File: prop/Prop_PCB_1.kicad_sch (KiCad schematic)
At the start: 13 parts

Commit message: finalize3pcb schematic
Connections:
- net SV1 is gone; now on net Sol1Lead1: J?.1
- net SV2 is gone; now on net Sol2Lead1: J?.3
- net Sol1Lead2: now also J?.2
- net Sol2Lead2: now also J?.4
- no-connect marks 39 -> 43
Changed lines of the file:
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@@
   (no_connect (at 54.61 40.64))
   (no_connect (at 54.61 43.18))
+  (no_connect (at 54.61 55.88))
+  (no_connect (at 54.61 58.42))
+  (no_connect (at 54.61 60.96))
+  (no_connect (at 54.61 66.04))
   (no_connect (at 82.55 58.42))
   (no_connect (at 54.61 83.82))
@@
   (no_connect (at 83.82 172.72))
   (no_connect (at 262.89 63.5))
-  (polyline (pts (xy 271.78 99.06) (xy 271.78 130.81))
+  (polyline (pts (xy 273.05 99.06) (xy 273.05 130.81))
     (stroke (width 0) (type default) (color 0 0 0 0))
   )
@@
     (stroke (width 0) (type default) (color 0 0 0 0))
   )
-  (wire (pts (xy 52.705 55.88) (xy 54.61 55.88))
-    (stroke (width 0) (type default) (color 0 0 0 0))
-  )
   (wire (pts (xy 262.89 53.34) (xy 264.795 53.34))
     (stroke (width 0) (type default) (color 0 0 0 0))
@@
     (stroke (width 0) (type default) (color 0 0 0 0))
   )
-  (polyline (pts (xy 43.18 100.33) (xy 111.76 100.33))
+  (polyline (pts (xy 39.37 100.33) (xy 111.76 100.33))
     (stroke (width 0) (type default) (color 0 0 0 0))
   )
@@
     (stroke (width 0) (type default) (color 0 0 0 0))
   )
-  (polyline (pts (xy 215.9 99.06) (xy 271.78 99.06))
-    (stroke (width 0) (type default) (color 0 0 0 0))
-  )
-  (wire (pts (xy 52.705 60.96) (xy 54.61 60.96))
+  (polyline (pts (xy 215.9 99.06) (xy 273.05 99.06))
     (stroke (width 0) (type default) (color 0 0 0 0))
   )
@@
     (stroke (width 0) (type default) (color 0 0 0 0))
   )
-  (polyline (pts (xy 215.9 83.82) (xy 271.78 83.82))
+  (polyline (pts (xy 212.09 83.82) (xy 274.32 83.82))
     (stroke (width 0) (type default) (color 0 0 0 0))
   )
@@
     (stroke (width 0) (type default) (color 0 0 0 0))
   )
+  (wire (pts (xy 232.41 148.59) (xy 236.22 148.59))
+    (stroke (width 0) (type default) (color 0 0 0 0))
+  )
   (wire (pts (xy 165.1 115.57) (xy 165.1 113.03))
     (stroke (width 0) (type default) (color 0 0 0 0))
@@
     (stroke (width 0) (type default) (color 0 0 0 0))
   )
-  (polyline (pts (xy 215.9 29.21) (xy 215.9 83.82))
-    (stroke (width 0) (type default) (color 0 0 0 0))
-  )
-  (polyline (pts (xy 43.18 26.67) (xy 43.18 100.33))
-    (stroke (width 0) (type default) (color 0 0 0 0))
-  )
-  (polyline (pts (xy 271.78 29.21) (xy 215.9 29.21))
+  (polyline (pts (xy 212.09 29.21) (xy 212.09 83.82))
+    (stroke (width 0) (type default) (color 0 0 0 0))
+  )
+  (polyline (pts (xy 39.37 26.67) (xy 39.37 100.33))
+    (stroke (width 0) (type default) (color 0 0 0 0))
+  )
+  (polyline (pts (xy 274.32 29.21) (xy 212.09 29.21))
     (stroke (width 0) (type default) (color 0 0 0 0))
   )
@@
     (stroke (width 0) (type default) (color 0 0 0 0))
   )
-  (wire (pts (xy 52.705 58.42) (xy 54.61 58.42))
-    (stroke (width 0) (type default) (color 0 0 0 0))
-  )
   (wire (pts (xy 95.25 68.58) (xy 82.55 68.58))
     (stroke (width 0) (type default) (color 0 0 0 0))
@@
     (stroke (width 0) (type default) (color 0 0 0 0))
   )
-  (polyline (pts (xy 271.78 83.82) (xy 271.78 29.21))
+  (polyline (pts (xy 274.32 83.82) (xy 274.32 29.21))
     (stroke (width 0) (type default) (color 0 0 0 0))
   )
@@
     (stroke (width 0) (type default) (color 0 0 0 0))
   )
-  (wire (pts (xy 52.705 66.04) (xy 54.61 66.04))
-    (stroke (width 0) (type default) (color 0 0 0 0))
-  )
   (wire (pts (xy 172.72 73.66) (xy 172.72 77.47))
     (stroke (width 0) (type default) (color 0 0 0 0))
@@
     (stroke (width 0) (type default) (color 0 0 0 0))
   )
-  (polyline (pts (xy 271.78 130.81) (xy 215.9 130.81))
+  (polyline (pts (xy 273.05 130.81) (xy 215.9 130.81))
     (stroke (width 0) (type default) (color 0 0 0 0))
   )
@@
     (stroke (width 0) (type default) (color 0 0 0 0))
   )
-  (polyline (pts (xy 111.76 26.67) (xy 43.18 26.67))
+  (polyline (pts (xy 111.76 26.67) (xy 39.37 26.67))
     (stroke (width 0) (type default) (color 0 0 0 0))
   )
@@
     (stroke (width 0) (type default) (color 0 0 0 0))
   )
+  (wire (pts (xy 232.41 153.67) (xy 236.22 153.67))
+    (stroke (width 0) (type default) (color 0 0 0 0))
+  )
   (wire (pts (xy 74.93 127) (xy 80.01 127))
     (stroke (width 0) (type default) (color 0 0 0 0))
@@
     )
   )
-  (global_label "SV1" (shape input) (at 236.22 146.05 0) (fields_autoplaced)
-    (effects (font (size 1.27 1.27)) (justify left))
-    (property "Intersheet References" "${INTERSHEET_REFS}" (id 0) (at 242.1407 145.9706 0)
-      (effects (font (size 1.27 1.27)) (justify left) hide)
-    )
-  )
-  (global_label "SV2" (shape input) (at 236.22 151.13 0) (fields_autoplaced)
-    (effects (font (size 1.27 1.27)) (justify left))
-    (property "Intersheet References" "${INTERSHEET_REFS}" (id 0) (at 242.1407 151.0506 0)
+  (global_label "Sol1Lead1" (shape input) (at 236.22 146.05 0) (fields_autoplaced)
+    (effects (font (size 1.27 1.27)) (justify left))
+    (property "Intersheet References" "${INTERSHEET_REFS}" (id 0) (at 248.4907 145.9706 0)
+      (effects (font (size 1.27 1.27)) (justify left) hide)
+    )
+  )
+  (global_label "Sol2Lead1" (shape input) (at 236.22 151.13 0) (fields_autoplaced)
+    (effects (font (size 1.27 1.27)) (justify left))
+    (property "Intersheet References" "${INTERSHEET_REFS}" (id 0) (at 248.4907 151.0506 0)
       (effects (font (size 1.27 1.27)) (justify left) hide)
     )
@@
     )
   )
-  (global_label "CS5" (shape input) (at 52.705 66.04 180) (fields_autoplaced)
-    (effects (font (size 1.27 1.27)) (justify right))
-    (property "Intersheet References" "${INTERSHEET_REFS}" (id 0) (at 46.6029 65.9606 0)
-      (effects (font (size 1.27 1.27)) (justify right) hide)
-    )
-  )
-  (global_label "CS3" (shape input) (at 52.705 60.96 180) (fields_autoplaced)
-    (effects (font (size 1.27 1.27)) (justify right))
-    (property "Intersheet References" "${INTERSHEET_REFS}" (id 0) (at 46.6029 60.8806 0)
-      (effects (font (size 1.27 1.27)) (justify right) hide)
-    )
-  )
   (global_label "Sol1" (shape input) (at 225.425 113.03 180) (fields_autoplaced)
     (effects (font (size 1.27 1.27)) (justify right))
@@
     )
   )
-  (global_label "CS2" (shape input) (at 52.705 58.42 180) (fields_autoplaced)
-    (effects (font (size 1.27 1.27)) (justify right))
-    (property "Intersheet References" "${INTERSHEET_REFS}" (id 0) (at 46.6029 58.3406 0)
-      (effects (font (size 1.27 1.27)) (justify right) hide)
-    )
-  )
   (global_label "Sol1_33" (shape input) (at 225.425 48.26 180) (fields_autoplaced)
     (effects (font (size 1.27 1.27)) (justify right))
@@
     )
   )
-  (global_label "CS1" (shape input) (at 52.705 55.88 180) (fields_autoplaced)
-    (effects (font (size 1.27 1.27)) (justify right))
-    (property "Intersheet References" "${INTERSHEET_REFS}" (id 0) (at 46.6029 55.8006 0)
-      (effects (font (size 1.27 1.27)) (justify right) hide)
-    )
-  )
   (global_label "PWM3_33" (shape input) (at 225.425 58.42 180) (fields_autoplaced)
     (effects (font (size 1.27 1.27)) (justify right))
@@
     )
   )
+  (global_label "Sol2Lead2" (shape input) (at 236.22 153.67 0) (fields_autoplaced)
+    (effects (font (size 1.27 1.27)) (justify left))
+    (property "Intersheet References" "${INTERSHEET_REFS}" (id 0) (at 248.4907 153.5906 0)
+      (effects (font (size 1.27 1.27)) (justify left) hide)
+    )
+  )
   (global_label "SPI0_SCK" (shape input) (at 52.705 53.34 180) (fields_autoplaced)
     (effects (font (size 1.27 1.27)) (justify right))
@@
       (effects (font (size 1.27 1.27)) (justify left) hide)
     )
+  )
+  (global_label "Sol1Lead2" (shape input) (at 236.22 148.59 0) (fields_autoplaced)
+    (effects (font (size 1.27 1.27)) (justify left))
+    (property "Intersheet References" "${INTERSHEET_REFS}" (id 0) (at 248.4907 148.5106 0)
+      (effects (font (size 1.27 1.27)) (justify left) hide)
+    )

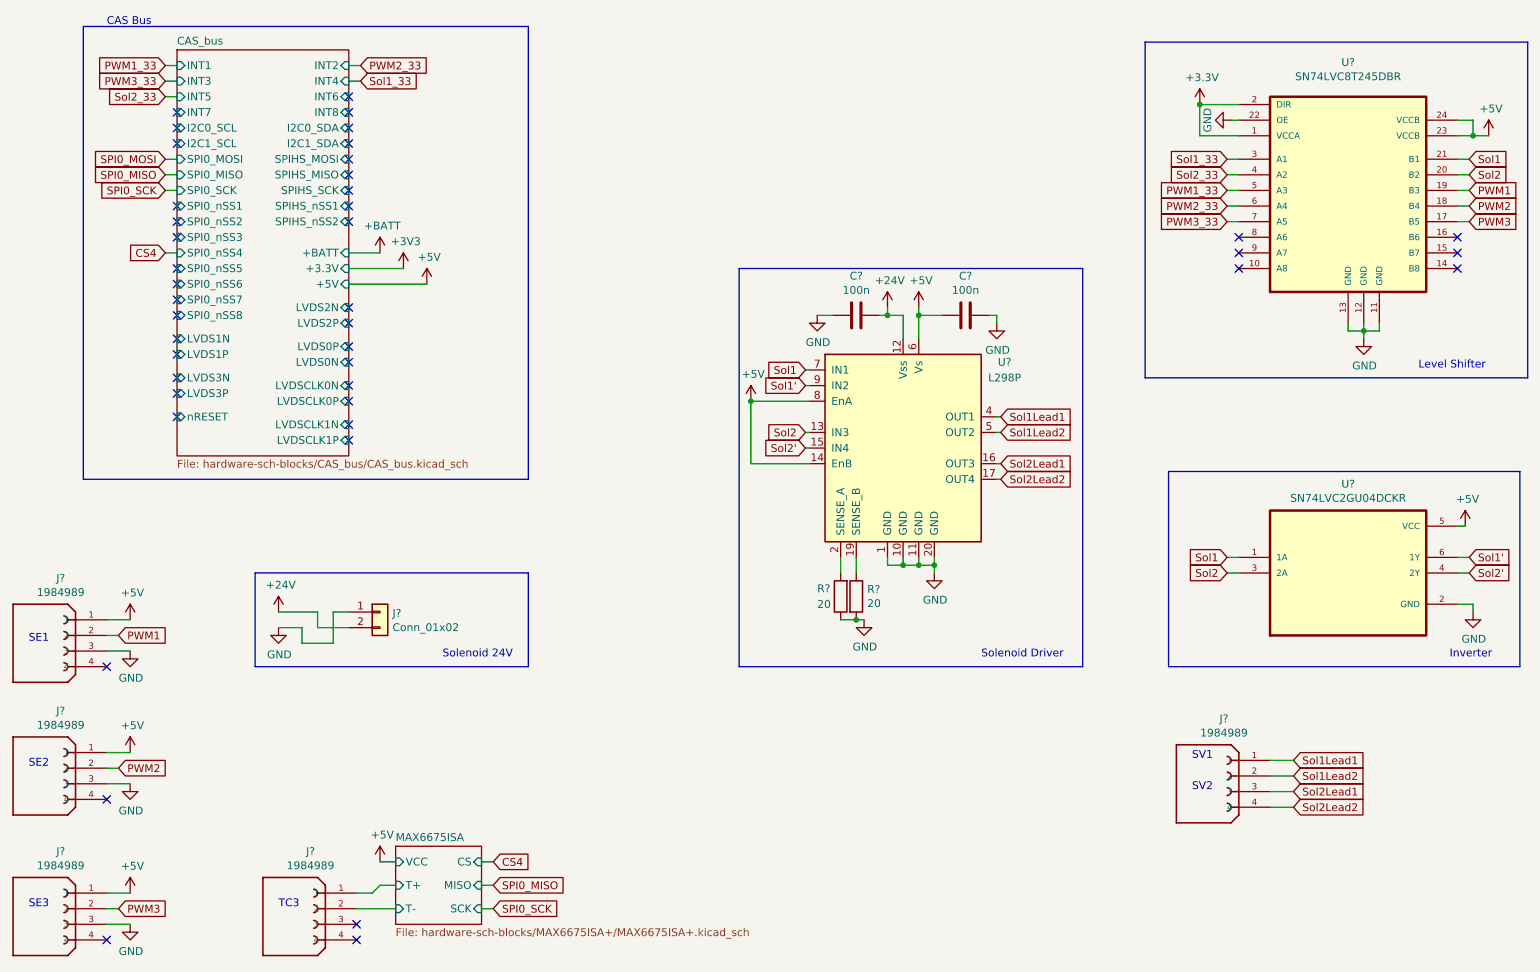
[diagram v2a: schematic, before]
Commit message: Connected power wires.
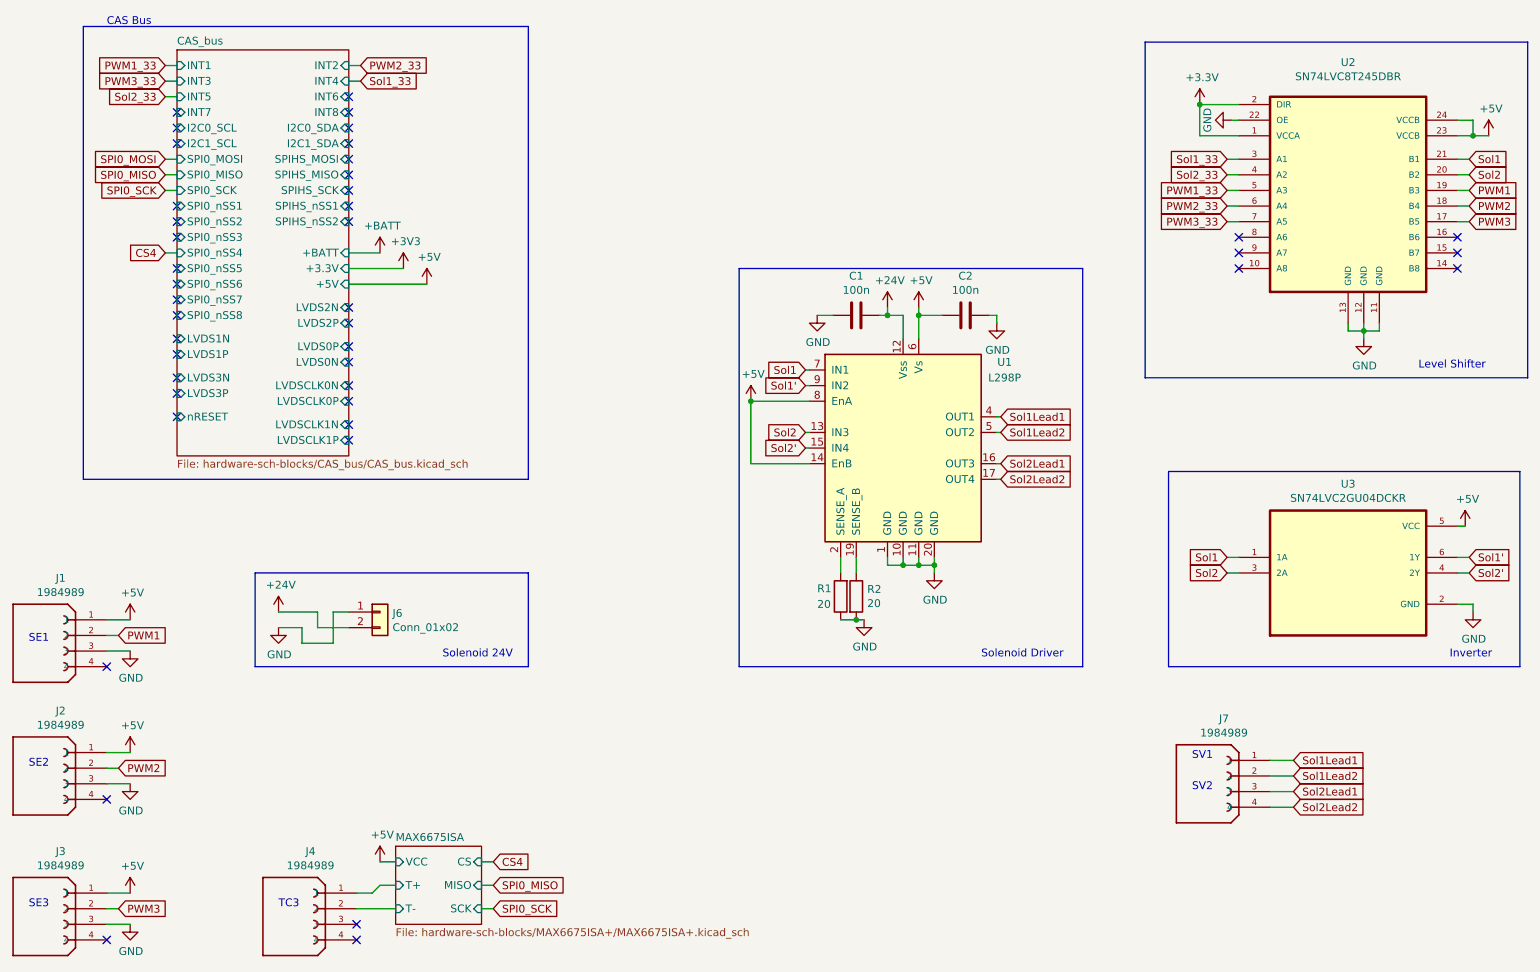
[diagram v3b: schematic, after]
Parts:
- gave numbers to parts that had none: 13
